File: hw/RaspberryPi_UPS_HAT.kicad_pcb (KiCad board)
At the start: 2 copper layers, 65 x 56 mm, 61 parts, among them J1 ISP, J2 Raspberry_Pi_2_3, J3 BAT, J4 COM, J5 FAN, J6 USB4125-GF-A_REVA, Q1 BC846, Q2 BC846, Q3 AO3401A, Q4 AO3401A, Q5 AO3401A, SW1 BTN, SW2 RST, U1 MIC5219-3.3YM5, U2 ATtiny841-SSU, U3 DS18B20, U4 MT3608, U5 LTC4054ES5-4.2

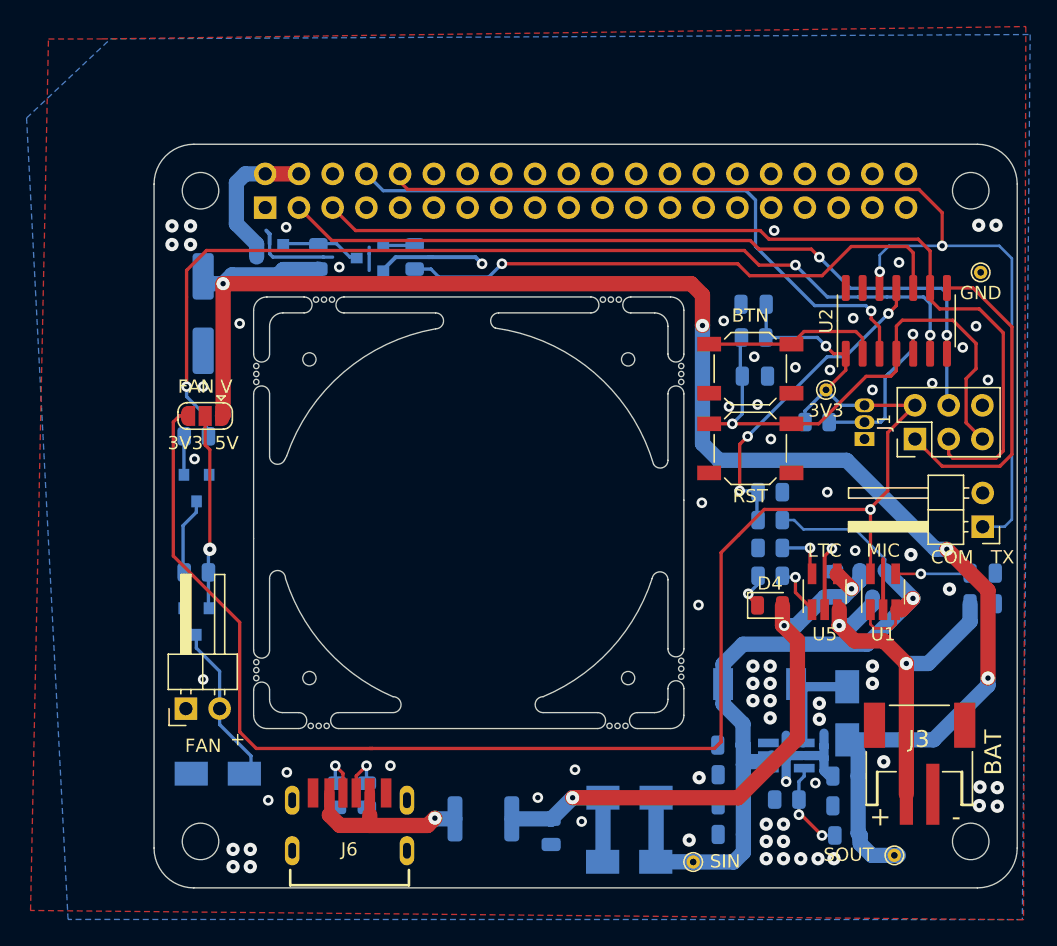
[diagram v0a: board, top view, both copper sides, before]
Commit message: update: make BTN available as optional pin header
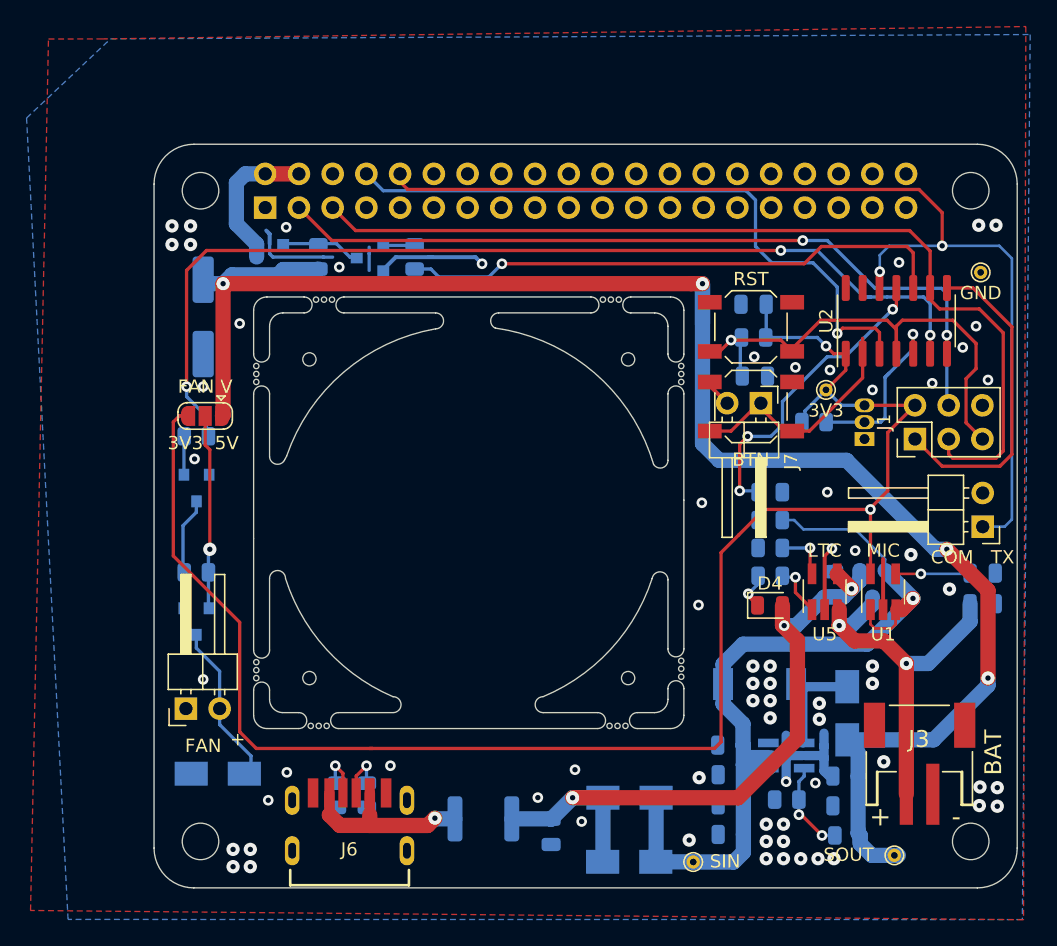
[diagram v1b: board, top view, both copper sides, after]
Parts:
- added J7: BTN, Connector_PinHeader_2.54mm:PinHeader_1x02_P2.54mm_Horizontal, F.Cu at (97.0, 58.0)
- moved SW2 9.15 mm to (96.2, 52.2), turned to 180 degrees
- moved SW1 2.85 mm to (96.2, 58.2), turned to 180 degrees
- moved C12 0.25 mm to (55.0, 51.5)
- moved R15 0.23 mm to (101.0, 59.4)
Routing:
- net BTN: track 13.3 -> 18.6 mm
- net /STEPUP_OUT_5V: track 124.3 -> 127.7 mm
- net GND: track 35.5 -> 37.7 mm, vias 74 -> 68
- net RST: track 40.9 -> 38.8 mm
- net /STEPUP_IN: track 65.4 -> 67.3 mm
- net RPI_IS_ONLINE_IN: track 47.8 -> 49.6 mm
- net STEPUP_VOLTAGE_IN: track 24.4 -> 25.4 mm
- net RPI_POWER_ON_OUT: track 42.3 -> 41.6 mm

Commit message: update: rev0.3 - new alignmant, LCSC listed elements
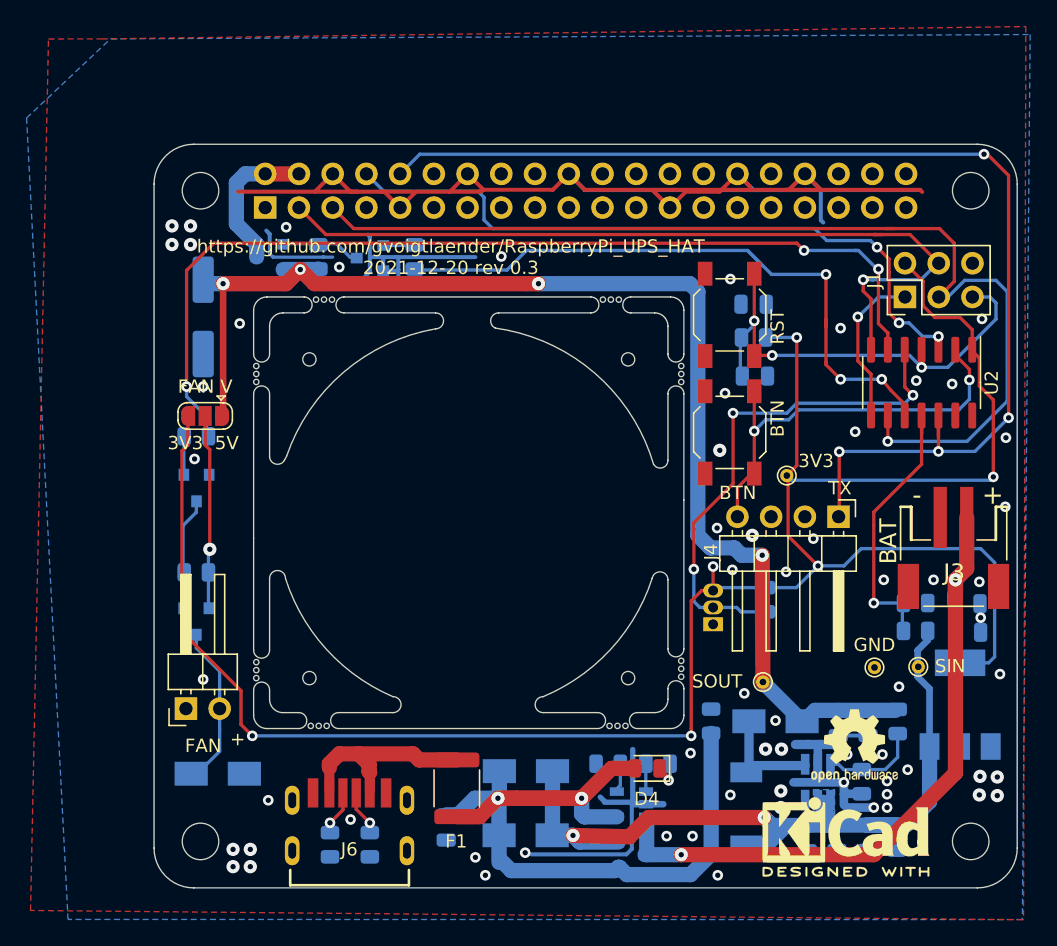
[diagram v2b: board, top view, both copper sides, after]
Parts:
- removed J7: BTN, Connector_PinHeader_2.54mm:PinHeader_1x02_P2.54mm_Horizontal
- added REF**: KiCad-Logo2_5mm_SilkScreen, Symbol:KiCad-Logo2_5mm_SilkScreen, F.Cu at (103.4, 90.7)
- added REF**: OSHW-Logo2_7.3x6mm_SilkScreen, Symbol:OSHW-Logo2_7.3x6mm_SilkScreen, F.Cu at (104.0, 83.8)
- F1: moved to F.Cu
- J2: footprint Connector_PinSocket_2.54mm:PinSocket_2x20_P2.54mm_Vertical -> RaspberryPi_UPS_HAT:PinSocket_2x20_P2.54mm_Vertical_RPI
- J4: footprint Connector_PinHeader_2.54mm:PinHeader_1x02_P2.54mm_Horizontal -> Connector_PinHeader_2.54mm:PinHeader_1x04_P2.54mm_Horizontal
- R12: value 1.5k -> 10k
- U1: value MIC5219-3.3YM5 -> AMS1117-3.3; footprint Package_TO_SOT_SMD:SOT-23-5_HandSoldering -> Package_TO_SOT_SMD:SOT-223-3_TabPin2; moved to B.Cu
- U5: value LTC4054ES5-4.2 -> TP4054; footprint Package_TO_SOT_SMD:SOT-23-5_HandSoldering -> Package_TO_SOT_SMD:SOT-23-5; moved to B.Cu
- moved TP3 30.8 mm to (105.5, 77.9)
- moved Q5 27.3 mm to (87.2, 92.0), turned to 0 degrees
- moved TP1 22.4 mm to (108.8, 77.8)
- moved U5 21.6 mm to (87.2, 88.2), turned to 180 degrees
- moved R12 20.3 mm to (85.5, 85.2)
- moved U3 18.0 mm to (93.4, 74.7)
- moved R13 16.5 mm to (89.2, 85.2), turned to 180 degrees
- moved TP2 16.4 mm to (97.2, 79.0)
- moved D4 15.4 mm to (88.4, 85.5), turned to 180 degrees
- moved R9 13.9 mm to (93.2, 82.0)
- moved R15 13.9 mm to (97.4, 72.8), turned to 270 degrees
- moved R1 13.8 mm to (108.7, 75.2)
- moved R2 13.8 mm to (108.7, 73.0)
- moved J3 13.7 mm to (111.5, 70.3), turned to 180 degrees
- moved C4 12.5 mm to (107.2, 90.7), turned to 270 degrees
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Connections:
- C1 pad 1: Net-(C1-Pad1) -> +3V3
- U1 pad 1: /STEPUP_IN -> GND
- U1 pad 2: GND -> +3V3
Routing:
- net GND: track 37.7 -> 174.2 mm, vias 68 -> 65
- net +3V3: track 127.4 -> 174.1 mm, vias 2 -> 6
- net /STEPUP_OUT_5V: track 127.7 -> 96.2 mm
- net ONE_WIRE: track 13.4 -> 39.0 mm, vias 1 -> 3
- net /V_BAT+: track 28.5 -> 49.7 mm
- net BTN: track 18.6 -> 31.5 mm, vias 0 -> 2
- net ISP_MISO: track 24.2 -> 12.2 mm, vias 0 -> 1
- net /5V_IN: track 51.2 -> 62.4 mm, vias 3 -> 2
- net TX: track 80.1 -> 89.0 mm, vias 2 -> 4
- net I2C_SCL: track 71.1 -> 78.9 mm, vias 0 -> 1
- net RPI_POWER_ON_OUT: track 41.6 -> 49.2 mm, vias 1 -> 3
- net /STEPUP_IN: track 67.3 -> 61.0 mm, vias 1 -> 2
- net Net-(C1-Pad1): track 5.62 -> 0.00 mm, vias 1 -> 0
- net RPI_IS_ONLINE_IN: track 49.6 -> 53.7 mm, vias 1 -> 3
- net STEPUP_VOLTAGE_IN: track 25.4 -> 21.5 mm, vias 3 -> 1
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- added copper zone on B.Cu, net /STEPUP_IN
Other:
- board text added: "BTN"
- board text added: "https://github.com/gvoigtlaender/RaspberryPi_UPS_HAT 2021-12-20 rev 0.3"
